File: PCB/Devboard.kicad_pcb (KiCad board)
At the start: 2 copper layers, 21 x 51 mm, 37 parts, among them J1 USB_C_Receptacle_USB2.0_14P, J2 Conn_01x20, J3 Conn_01x20, J4 Conn_01x03, SW1 SW_Push, U1 RP2040, U3 W25Q128JVS, U4 MCP1700x-330xxTT, Y1 12 MHz

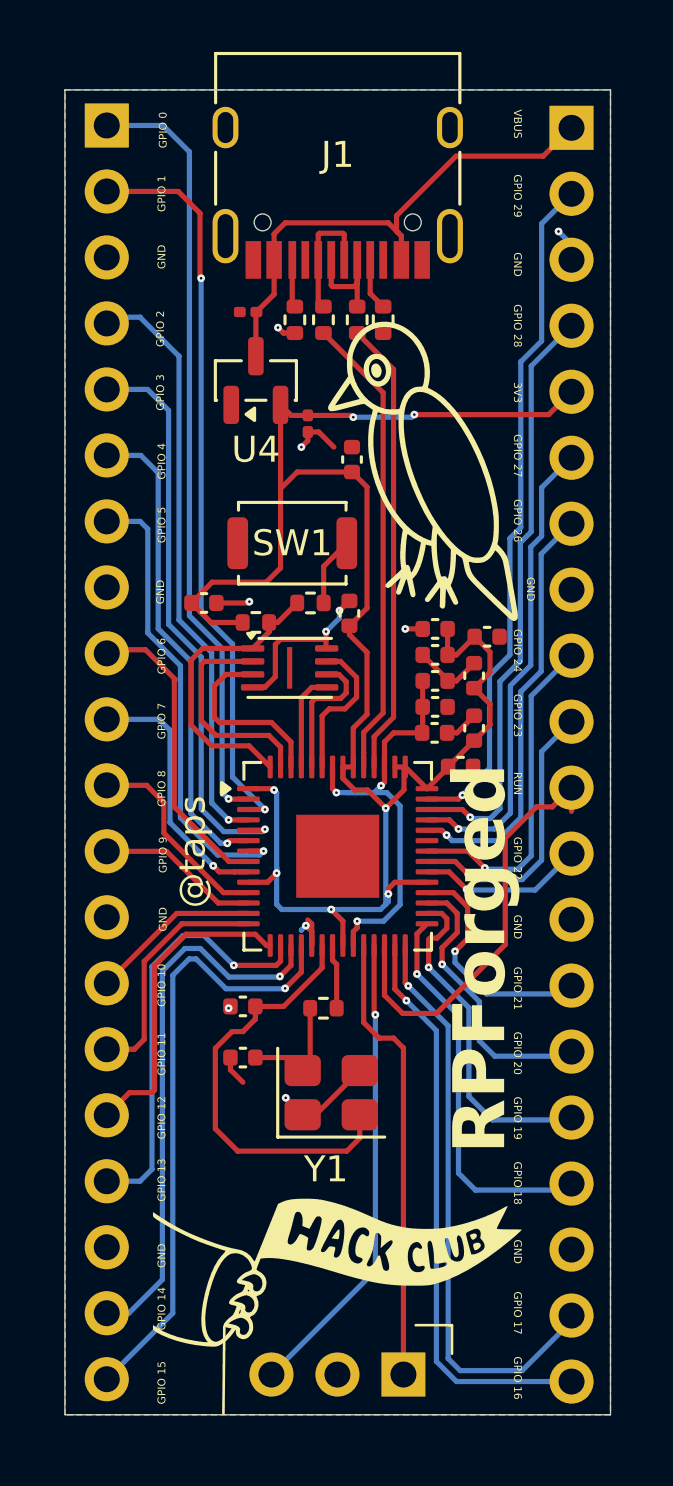
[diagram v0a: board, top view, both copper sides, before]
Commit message: updated pcb with vias insted of micro vias
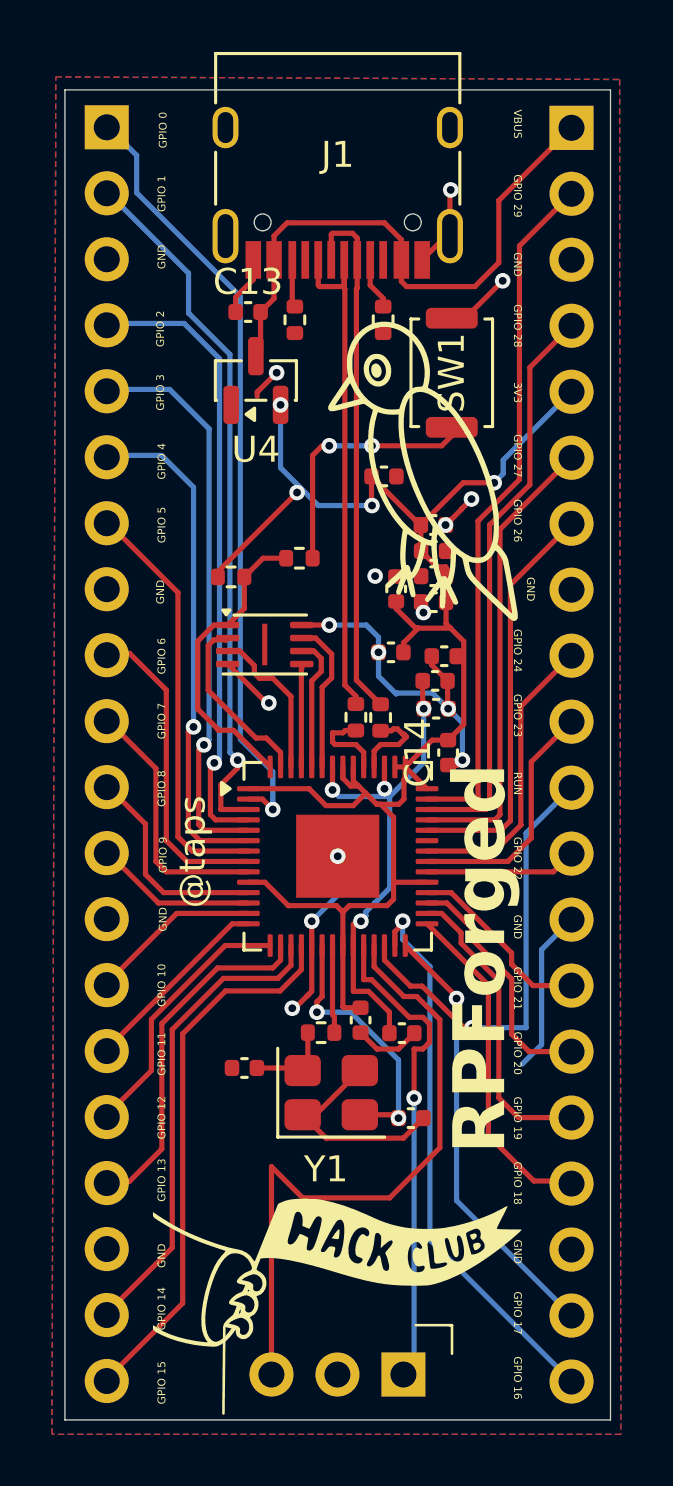
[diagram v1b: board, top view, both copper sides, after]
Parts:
- C13, C14: footprint Capacitor_SMD:C_0201_0603Metric -> Capacitor_SMD:C_0402_1005Metric
- moved R3 15.4 mm to (67.0, 44.9)
- moved R4 15.3 mm to (67.9, 44.9)
- moved C8 14.0 mm to (67.1, 56.6), turned to -90 degrees
- moved C14 13.8 mm to (70.5, 46.3)
- moved C2 12.6 mm to (68.7, 57.1)
- moved SW1 8.99 mm to (70.6, 31.6), turned to -90 degrees
- moved C10 8.36 mm to (69.9, 38.5)
- moved C16 7.77 mm to (69.1, 60.3), turned to 0 degrees
- moved C17 7.42 mm to (68.5, 40.0), turned to 90 degrees
- moved C6 4.77 mm to (69.9, 37.5)
- moved C5 3.00 mm to (70.3, 42.5), turned to 180 degrees
- moved C9 2.19 mm to (68.3, 42.4), turned to 180 degrees
- moved C11 2.03 mm to (69.9, 39.5)
- moved C7 2.03 mm to (69.9, 40.5)
- moved R6 2.00 mm to (62.1, 39.5)
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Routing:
- net GND: track 23.7 -> 49.5 mm, vias 10 -> 14
- net D -: track 4.75 -> 20.4 mm
- net D +: track 4.87 -> 20.3 mm
- net Net-(U1-USB_DP): track 18.0 -> 3.21 mm
- net Net-(U1-USB_DM): track 17.6 -> 3.24 mm
- net +3V3: track 75.2 -> 66.3 mm, vias 7 -> 4
- net Net-(R7-Pad2): track 2.67 -> 9.95 mm, vias 0 -> 2
- net SWD: track 18.2 -> 24.9 mm, vias 1 -> 0
- net XIN: track 16.7 -> 10.3 mm, vias 0 -> 2
- net GPI 17: track 22.5 -> 16.9 mm
- net GPI 14: track 21.3 -> 18.3 mm, vias 1 -> 0
- net +1V1: track 17.2 -> 20.1 mm, vias 3 -> 4
- net GPI 13: track 16.3 -> 13.6 mm, vias 1 -> 0
- net GPI 15: track 23.6 -> 21.0 mm, vias 1 -> 0
- net VBUS: track 20.0 -> 22.5 mm
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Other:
- board size 21 x 51 mm -> 21 x 51.2 mm
